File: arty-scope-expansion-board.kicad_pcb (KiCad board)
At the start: 4 copper layers, 109 x 75.5 mm, 136 parts, among them J1 PMOD_A, J2 PMOD_B, J3 PMOD_C, J4 PMOD_D, J5 Conn_Coaxial, J6 Conn_01x02_Pin, J7 Conn_Coaxial, U1 AD9288, U10 MCP1826S, U11 MIC5504-3.3YM5, U12 AD8132ARZ, U13 AD8370AREZ-RL7, U14 AD8132ARZ, U2 74LS374, U3 74LS374, U4 AD8370AREZ-RL7, U5 AD8132ARZ, U6 AD8132ARZ, U7 MCP4822, U8 74AHCT541, U9 74AHCT541

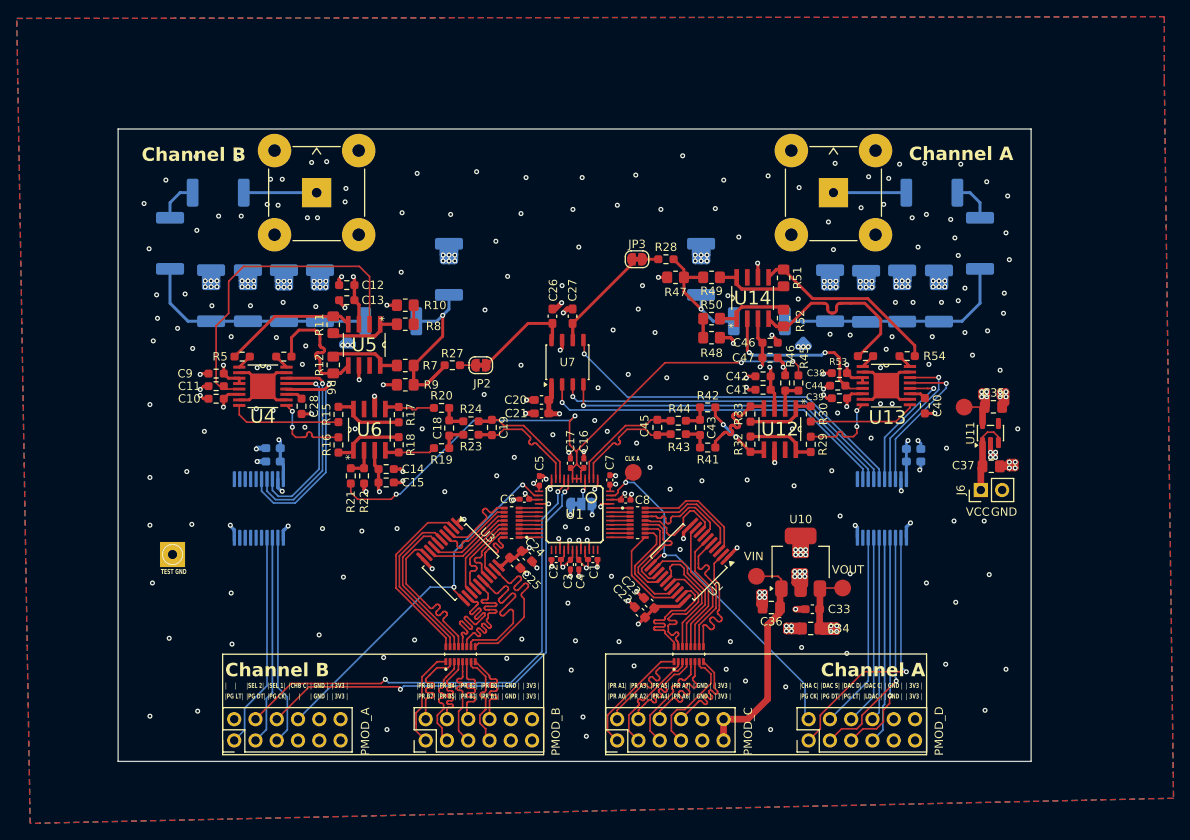
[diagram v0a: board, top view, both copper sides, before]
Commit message: [feat] Repaired some silkscreen errors and added some labels
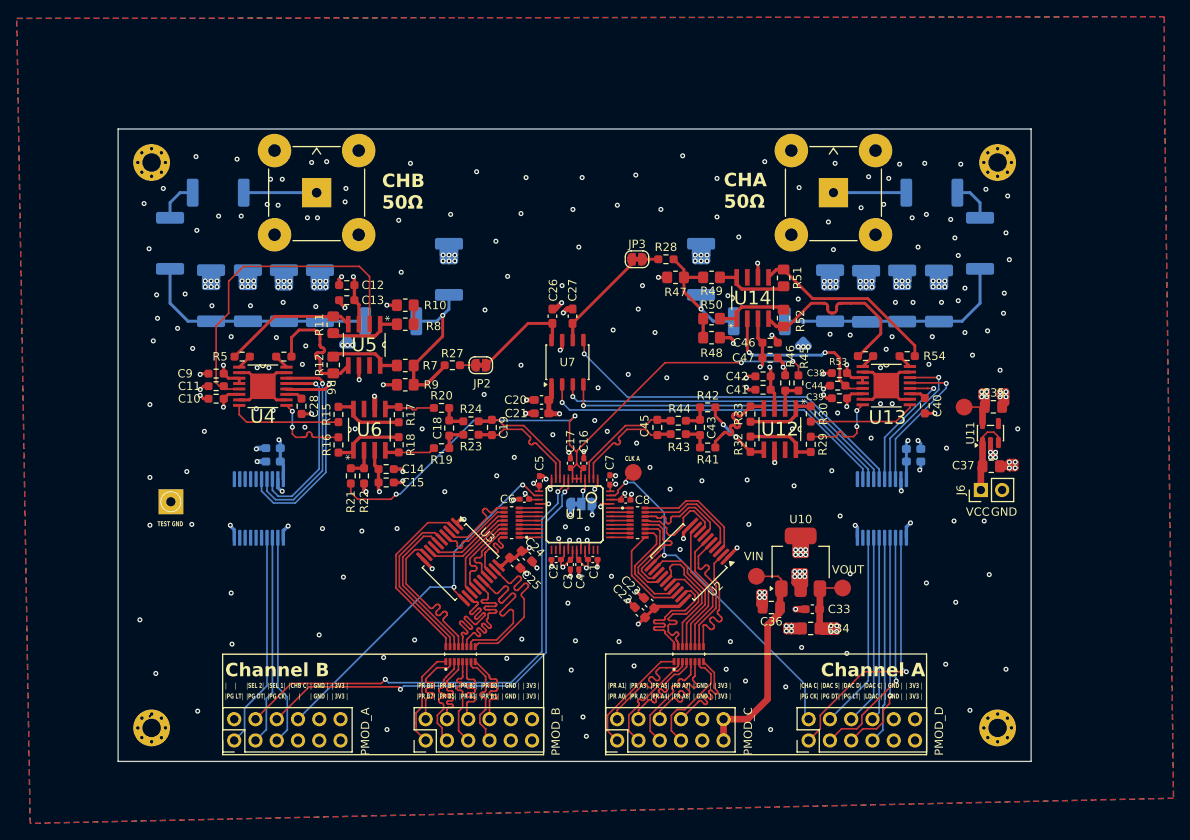
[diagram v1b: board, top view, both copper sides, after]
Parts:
- added REF**: MountingHole_2.2mm_M2_Pad_Via, MountingHole:MountingHole_2.2mm_M2_Pad_Via, F.Cu at (119.5, 51.5)
- added REF**: MountingHole_2.2mm_M2_Pad_Via, MountingHole:MountingHole_2.2mm_M2_Pad_Via, F.Cu at (119.5, 119.0)
- added REF**: MountingHole_2.2mm_M2_Pad_Via, MountingHole:MountingHole_2.2mm_M2_Pad_Via, F.Cu at (220.5, 51.5)
- added REF**: MountingHole_2.2mm_M2_Pad_Via, MountingHole:MountingHole_2.2mm_M2_Pad_Via, F.Cu at (220.5, 119.0)
- moved REF** 6.30 mm to (121.8, 92.0)
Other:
- board text added: "CHA 50Ω"
- board text added: "CHB 50Ω"
